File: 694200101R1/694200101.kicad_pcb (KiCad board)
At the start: 2 copper layers, 438.6 x 125.8 mm, 390 parts, among them J1 USB4085-GF-A, J2 Conn_01x05_Male, J3 Conn_01x02_Male, SW1 MX_SW, SW10 MX_SW, SW100 MX_SW, SW101 MX_SW, SW102 MX_SW, SW103 MX_SW, SW104 MX_SW, SW105 MX_SW, SW106 MX_SW, SW107 MX_SW, SW11 MX_SW, SW12 MX_SW, SW13 MX_SW, SW14 MX_SW, SW15 MX_SW, SW16 MX_SW, SW17 MX_SW, SW18 MX_SW, SW19 MX_SW, SW2 MX_SW, SW20 MX_SW, SW21 MX_SW, SW22 MX_SW, SW23 MX_SW, SW24 MX_SW, SW25 MX_SW, SW26 MX_SW, SW27 MX_SW, SW28 MX_SW, SW29 MX_SW, SW3 MX_SW, SW30 MX_SW, SW31 MX_SW, SW32 MX_SW, SW33 MX_SW, SW34 MX_SW, SW35 MX_SW, SW36 MX_SW, SW37 MX_SW, SW38 MX_SW, SW39 MX_SW, SW4 MX_SW, SW40 MX_SW, SW41 MX_SW, SW42 MX_SW, SW43 MX_SW, SW44 MX_SW, SW45 MX_SW, SW46 MX_SW, SW47 MX_SW, SW48 MX_SW, SW49 MX_SW, SW5 MX_SW, SW50 MX_SW, SW51 MX_SW, SW52 MX_SW, SW53 MX_SW, SW54 MX_SW, SW55 MX_SW, SW56 MX_SW, SW57 MX_SW, SW58 MX_SW, SW59 MX_SW, SW6 MX_SW, SW60 MX_SW, SW61 MX_SW, SW62 MX_SW, SW63 MX_SW, SW64 MX_SW, SW65 MX_SW, SW66 MX_SW, SW67 MX_SW, SW68 MX_SW, SW69 MX_SW, SW7 MX_SW, SW70 MX_SW, SW71 MX_SW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

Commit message: routed LED fir driver 1
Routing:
- net SW3_A: track 0.00 -> 375.0 mm, vias 0 -> 2
- net SW2_A: track 0.00 -> 373.3 mm, vias 0 -> 2
- net SW1_A: track 0.00 -> 373.0 mm, vias 0 -> 2
- net SW6_A: track 0.00 -> 285.8 mm
- net SW5_A: track 0.00 -> 285.8 mm
- net SW4_A: track 0.00 -> 285.8 mm
- net SW7_A: track 171.5 -> 274.4 mm
- net SW8_A: track 171.4 -> 274.4 mm
- net SW9_A: track 171.5 -> 274.3 mm

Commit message: LED traces driver 2 row 1-2
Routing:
- net SW12_B: track 0.00 -> 291.7 mm, vias 0 -> 1
- net SW11_B: track 0.00 -> 288.8 mm, vias 0 -> 1
- net SW10_B: track 0.00 -> 286.2 mm, vias 0 -> 1
- net SW7_B: track 0.00 -> 280.2 mm, vias 0 -> 1
- net SW8_B: track 0.00 -> 279.0 mm, vias 0 -> 1
- net SW9_B: track 0.00 -> 278.8 mm, vias 0 -> 1

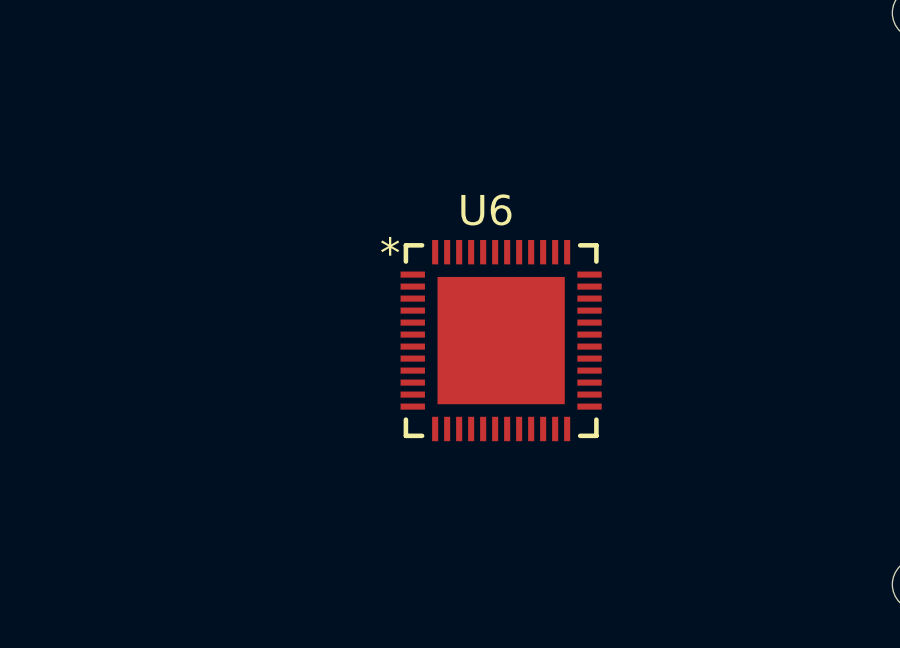
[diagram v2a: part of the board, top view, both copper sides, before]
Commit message: Update 694200101.kicad_pcb
update led driver location
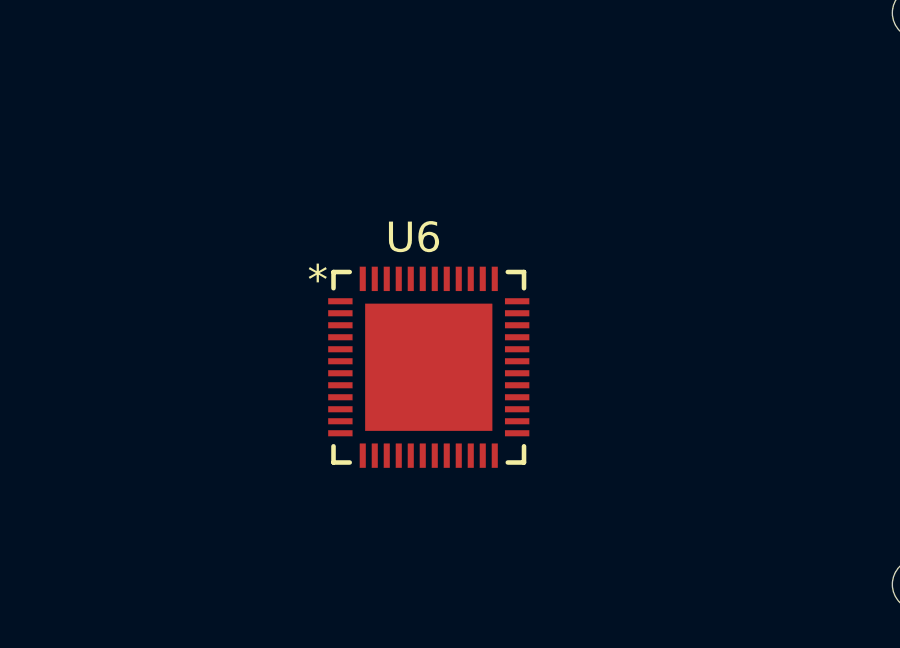
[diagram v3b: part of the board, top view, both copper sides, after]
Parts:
- moved U6 2.57 mm to (345.6, 88.0)
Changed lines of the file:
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@@
   )
   (module Lumissil:IS31FL3733B-QFLS4-TR (layer F.Cu)
-    (at 347.98 87.122)
+    (at 345.567 88.011)
     (attr smd)
     (fp_text reference U6 (at -0.508 -4.318) (layer F.SilkS)

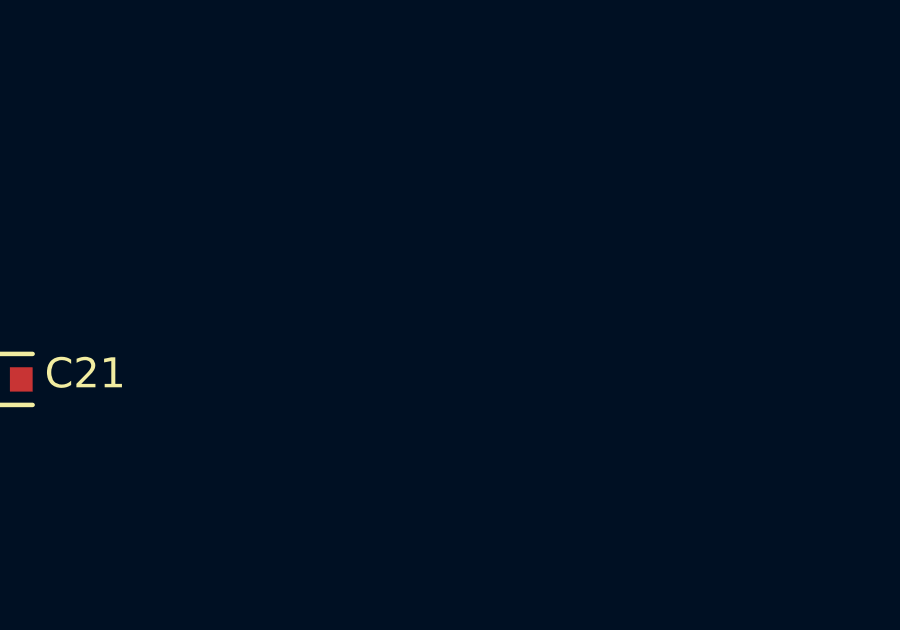
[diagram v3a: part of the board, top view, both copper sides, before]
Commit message: Updated USB C protection Circuit
Added PTC fuse and choke for surge suppression.
Added ferrite bead to reduce coupling
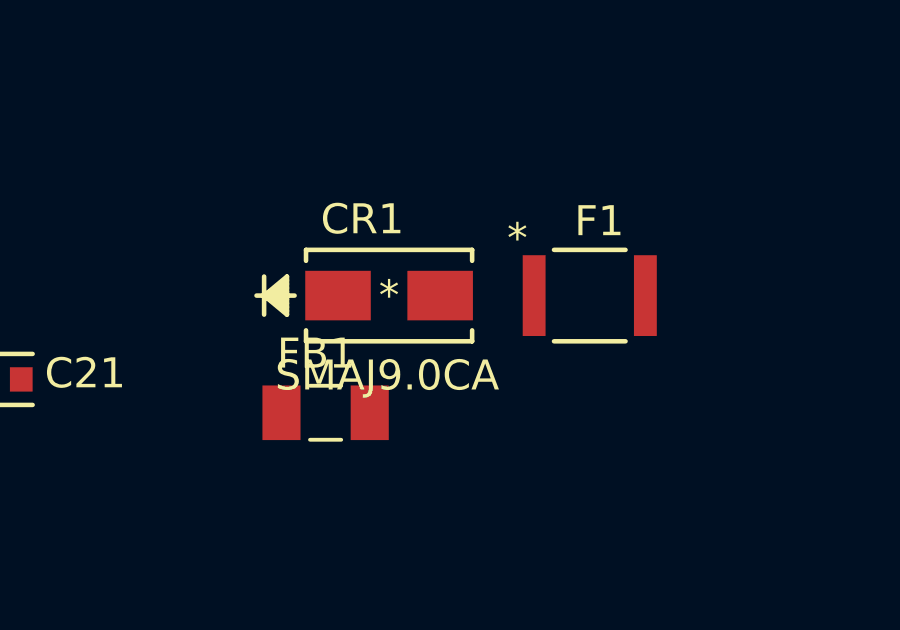
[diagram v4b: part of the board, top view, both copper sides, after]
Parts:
- added CR1: SMAJ9.0CA, Littlefuse:SMAJ9.0CA, F.Cu at (380.1, 178.2)
- added F1: 1210L150THWR, Littlefuse:1210L150THWR, F.Cu at (386.8, 178.2)
- added FB1: FBMJ3216HM600-T, Taiyo Yuden:BEADC3216X130N, F.Cu at (378.0, 182.2)
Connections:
- C1 pad 2: GND -> Earth
- J1 pad 1: GND -> Earth
- J1 pad 2: GND -> Earth
- J1 pad 3: GND -> Earth
- J1 pad 4: GND -> Earth
- J1 pad A1: GND -> Earth
- J1 pad A12: GND -> Earth
- J1 pad B1: GND -> Earth
- J1 pad B12: GND -> Earth
- R1 pad 2: GND -> Earth
- R2 pad 2: GND -> Earth
- U1 pad 1: +5V -> VCC
- U2 pad 2: GND -> Earth

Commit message: relaing usb
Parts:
- CR1, F1, FB1: moved to B.Cu
- moved C18 217.0 mm to (389.3, -24.3)
- moved C19 217.0 mm to (369.0, -27.3)
- moved C20 217.0 mm to (395.8, -21.2)
- moved C21 217.0 mm to (398.3, -33.7)
- moved C24 217.0 mm to (369.2, -22.8)
- moved R19 217.0 mm to (369.4, -30.0)
- moved R20 217.0 mm to (356.9, -26.4)
- moved C22 217.0 mm to (399.3, -13.3)
- moved C23 217.0 mm to (391.5, -29.3)
- moved R18 217.0 mm to (376.9, -24.4)
- moved CR1 184.8 mm to (376.3, -6.48)
- moved F1 182.0 mm to (366.6, -2.67)
- moved FB1 170.9 mm to (358.1, 12.4), turned to 180 degrees

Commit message: update led footprint
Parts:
- moved FB1 7.62 mm to (350.5, 12.3), turned to 90 degrees
- moved F1 7.44 mm to (363.2, 3.94), turned to 90 degrees
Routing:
- net +5V: track 53.6 -> 17.8 mm, vias 5 -> 1
- net VCC: track 0.00 -> 32.4 mm, vias 0 -> 4

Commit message: trying to fix fb1
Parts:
- FB1: value FBMJ3216HM600-T -> BBUP00160808600Y00; footprint Taiyo Yuden:BEADC3216X130N -> Resistor-Libs:Yageo-RC0603-0-0-IPC_C
- moved FB1 18.7 mm to (357.1, -5.21), turned to 180 degrees
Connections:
- FB1 pad 1: GND -> (no net)
- FB1 pad 2: Earth -> (no net)

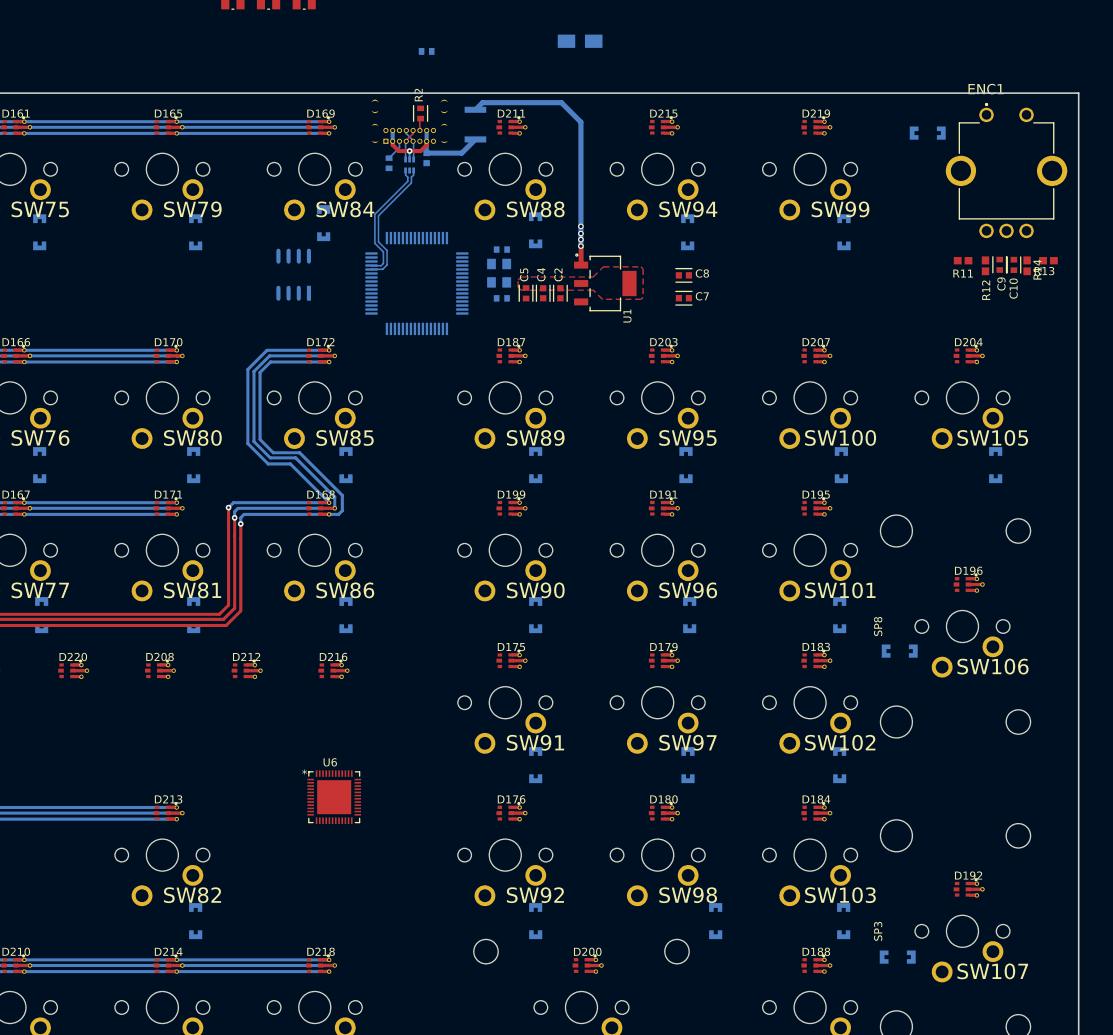
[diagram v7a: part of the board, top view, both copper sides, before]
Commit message: all LED rows
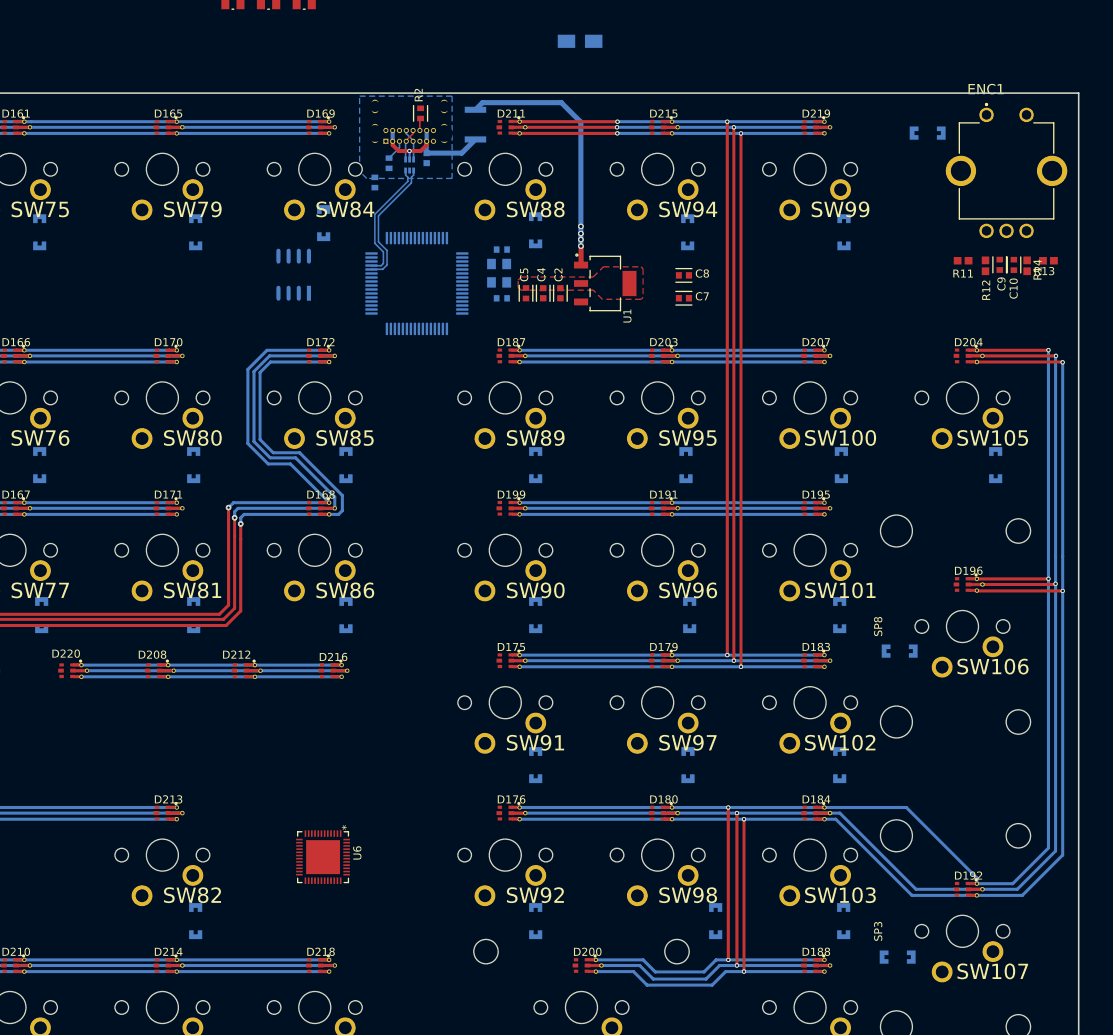
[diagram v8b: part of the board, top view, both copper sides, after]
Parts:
- moved FB1 17.6 mm to (350.6, 11.2), turned to 90 degrees
- moved U6 7.62 mm to (344.2, 95.5), turned to 270 degrees
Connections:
- FB1 pad 1: (no net) -> GND
- FB1 pad 2: (no net) -> Earth
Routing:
- net SW3_B: track 0.00 -> 238.6 mm, vias 0 -> 4
- net SW2_B: track 0.00 -> 234.0 mm, vias 0 -> 4
- net SW1_B: track 0.00 -> 233.9 mm, vias 0 -> 4
- net SW6_B: track 0.00 -> 219.1 mm, vias 0 -> 3
- net SW5_B: track 0.00 -> 219.1 mm, vias 0 -> 3
- net SW4_B: track 0.00 -> 219.1 mm, vias 0 -> 3
- added copper zone on B.Cu, net Earth
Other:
- net class Default: via_dia 0.8 -> 0.5588; via_drill 0.4 -> 0.3048
